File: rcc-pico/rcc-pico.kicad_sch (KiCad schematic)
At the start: 24 parts, among them J1 PJ-006A, J2 Conn_01x03_Female, SW1 SW_Push, U1 AP63300WU-7, U2 PicoW, U3 Conn_03x20, U4 Conn_03x20

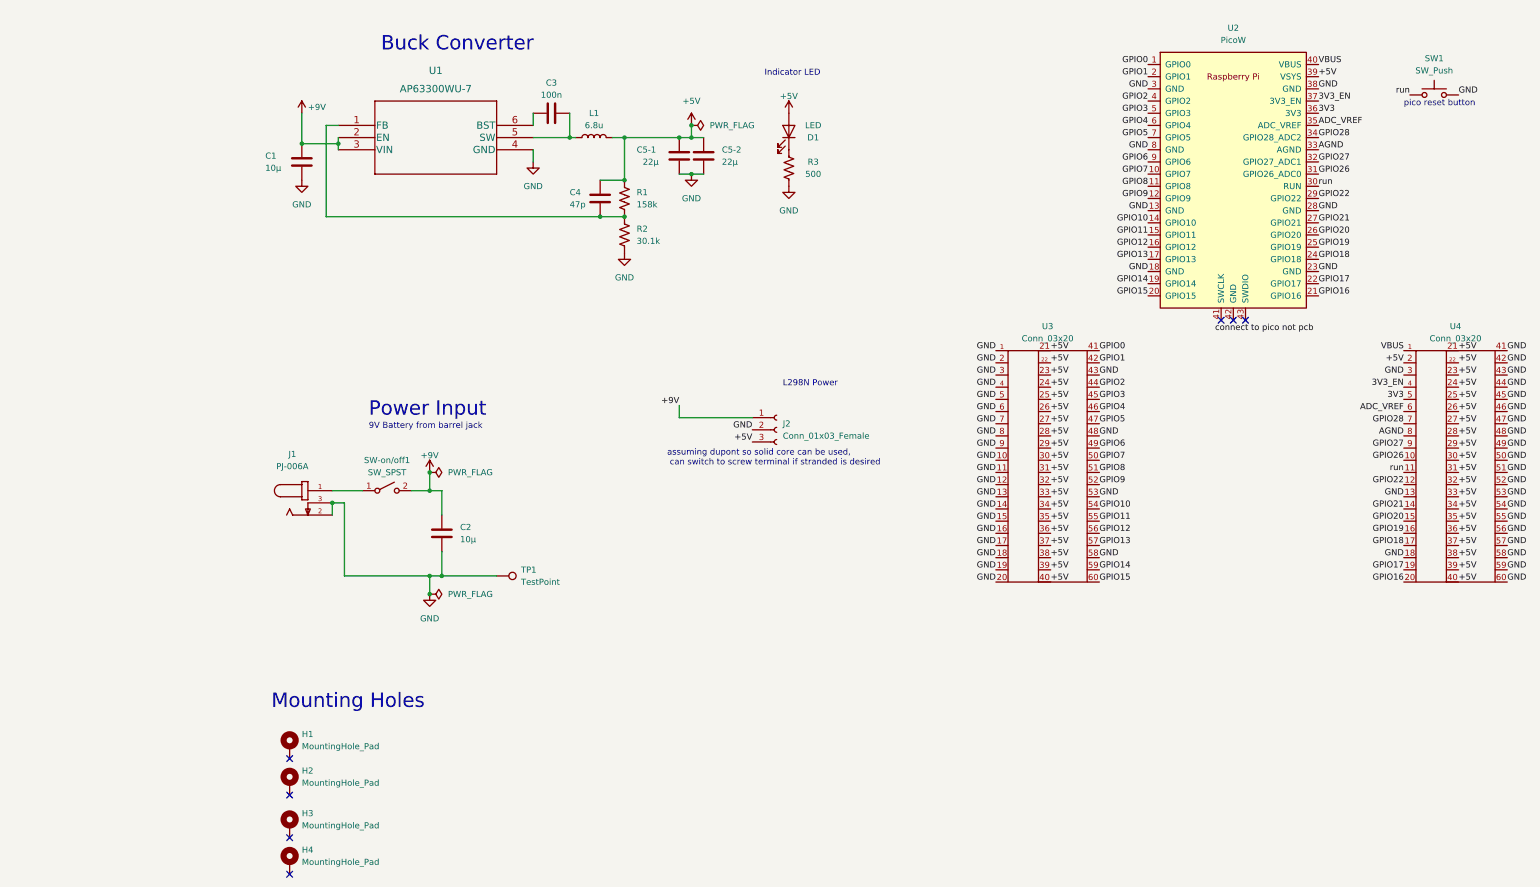
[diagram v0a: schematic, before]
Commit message: new schematic with LDO
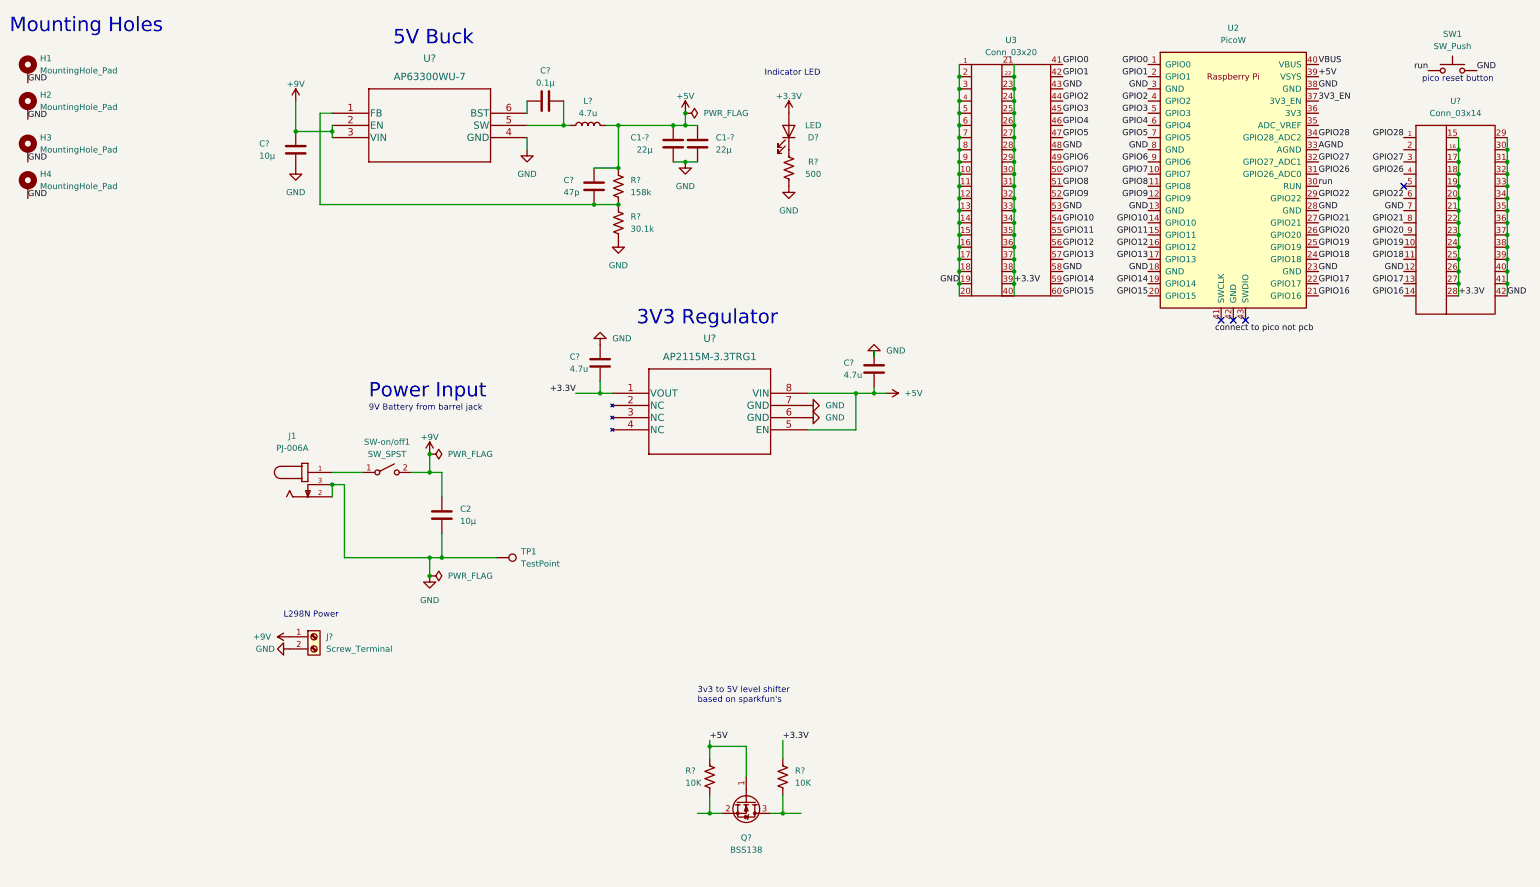
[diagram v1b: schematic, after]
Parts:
- removed C1: 10μ, Capacitor_SMD:C_1210_3225Metric_Pad1.33x2.70mm_HandSolder, symbol Device:C
- removed C3: 100n, Capacitor_SMD:C_1206_3216Metric_Pad1.33x1.80mm_HandSolder, symbol Device:C
- removed C4: 47p, Capacitor_SMD:C_0603_1608Metric_Pad1.08x0.95mm_HandSolder, symbol Device:C
- removed C5-1, C5-2: 22μ, Capacitor_SMD:C_1210_3225Metric_Pad1.33x2.70mm_HandSolder, symbol Device:C
- removed D1: LED, LED_SMD:LED_0603_1608Metric, symbol Device:LED
- removed J2: Conn_01x03_Female, Connector_PinHeader_2.54mm:PinHeader_1x03_P2.54mm_Vertical, symbol Connector:Conn_01x03_Female
- removed L1: 6.8u, Inductor_SMD:L_Wuerth_HCI-1365, symbol Device:L
- removed R1: 158k, Resistor_SMD:R_0805_2012Metric_Pad1.20x1.40mm_HandSolder, symbol Device:R_US
- removed R2: 30.1k, Resistor_SMD:R_1206_3216Metric, symbol Device:R_US
- removed R3: 500, Resistor_SMD:R_0603_1608Metric, symbol Device:R_US
- removed U1: AP63300WU-7, Package_TO_SOT_SMD:TSOT-23-6_HandSoldering, symbol ultralibrarian:AP63300WU-7
- removed U4: Conn_03x20, 3rdparty:PinHeader_3x20_P2.54mm_Vertical, symbol Connector:Conn_03x20
- added C1-? (x2): 22μ, Capacitor_SMD:C_1210_3225Metric_Pad1.33x2.70mm_HandSolder, symbol Device:C
- added C?: 10μ, Capacitor_SMD:C_1210_3225Metric_Pad1.33x2.70mm_HandSolder, symbol Device:C
- added C?: 0.1μ, Capacitor_SMD:C_1206_3216Metric_Pad1.33x1.80mm_HandSolder, symbol Device:C
- added C? (x2): 4.7u, Capacitor_SMD:C_0603_1608Metric_Pad1.08x0.95mm_HandSolder, symbol Device:C
- added C?: 47p, Capacitor_SMD:C_0603_1608Metric_Pad1.08x0.95mm_HandSolder, symbol Device:C
- added D?: LED, LED_SMD:LED_0603_1608Metric, symbol Device:LED
- added J?: Screw_Terminal, TerminalBlock_4Ucon:TerminalBlock_4Ucon_1x02_P3.50mm_Horizontal, symbol Connector:Screw_Terminal_01x02
- added L?: 4.7u, Inductor_SMD:SIDMP-SP0530, symbol Device:L
- added Q?: BSS138, Package_TO_SOT_SMD:SOT-23, symbol Transistor_FET:BSS138
- added R?: 500, Resistor_SMD:R_0603_1608Metric, symbol Device:R_US
- added R?: 158k, Resistor_SMD:R_0805_2012Metric_Pad1.20x1.40mm_HandSolder, symbol Device:R_US
- added R?: 30.1k, Resistor_SMD:R_1206_3216Metric, symbol Device:R_US
- added R? (x2): 10K, Resistor_SMD:R_1206_3216Metric, symbol Device:R_US
- added U?: AP2115M-3.3TRG1, Package_SO:AP2115M-3.3TRG1, symbol Regulator_Linear:AP2115M-3.3TRG1
- added U?: Conn_03x14, symbol Connector:Conn_03x14
- added U?: AP63300WU-7, Package_TO_SOT_SMD:TSOT-23-6_HandSoldering, symbol ultralibrarian:AP63300WU-7
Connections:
- net +5V: now also C1-?.1, C1-?.1, C?.1, C?.2, L?.2, Q?.1 (G), R?.1, R?.2, U?.5 (EN), U?.8 (VIN); no longer U3.21, U3.22, U3.23, U3.24, U3.25, U3.26, U3.27, U3.28, U3.29, U3.30, U3.31, U3.32, U3.33, U3.34, U3.35, U3.36, U3.37, U3.38, U3.39, U3.40
- net +9V: now also C?.1, J?.1 (Pin_1), U?.2 (EN), U?.3 (VIN)
- net GND: now also H1.1, H2.1, H3.1, H4.1, C1-?.2, C1-?.2, C?.2, C?.2, C?.2, J?.2 (Pin_2), R?.2, R?.2, U?.12, U?.29, U?.30, U?.31, U?.32, U?.33, U?.34, U?.35, U?.36, U?.37, U?.38, U?.39, U?.4 (GND), U?.40, U?.41, U?.42, U?.6 (GND), U?.7, U?.7 (GND)
- net GPIO16: now also U?.14
- net GPIO17: now also U?.13
- net GPIO18: now also U?.11
- net GPIO19: now also U?.10
- net GPIO20: now also U?.9
- net GPIO21: now also U?.8
- net GPIO22: now also U?.6
- net GPIO26: now also U?.4
- net GPIO27: now also U?.3
- net GPIO28: now also U?.1
- net 3V3: no longer names the net of U2.36 (3V3)
- net ADC_VREF: no longer names the net of U2.35 (ADC_VREF)
- new net: Q?.2 (S), R?.2
- new net: Q?.3 (D), R?.2
- new net: C?.2, L?.1, U?.5 (SW)
- new net: D?.1 (K), R?.1
- new net: C?.1, R?.1, R?.1, U?.1 (FB)
- new net: C?.1, U?.6 (BST)
- new net +3.3V: C?.1, D?.2 (A), R?.1, U3.21, U3.22, U3.23, U3.24, U3.25, U3.26, U3.27, U3.28, U3.29, U3.30, U3.31, U3.32, U3.33, U3.34, U3.35, U3.36, U3.37, U3.38, U3.39, U3.40, U?.1 (VOUT), U?.15, U?.16, U?.17, U?.18, U?.19, U?.20, U?.21, U?.22, U?.23, U?.24, U?.25, U?.26, U?.27, U?.28
- no-connect marks 7 -> 4
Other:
- note added: "3V3 Regulator"
- note added: "3v3 to 5V level shifter based on sparkfun's"
- note added: "5V Buck"
- note removed: "Buck Converter"
- note removed: "assuming dupont so solid core can be used, can switch to screw terminal if stranded is desired"
- moved on the sheet: C2, H1, H2, H3, H4, J1, SW-on/off1, SW1, TP1, U3

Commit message: finished schematic
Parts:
- added J10: Conn_3x3_female, Connector_PinHeader_2.54mm:PinHeader3x3_P2.54mm_Vertical, symbol Connector:Conn_3x3_female
- added J3, J7: Conn_02x03_Top_Bottom, Connector_PinHeader_2.54mm:PinHeader_2x03_P2.54mm_Vertical, symbol Connector_Generic:Conn_02x03_Odd_Even
- added J4, J6: Conn_03x3_female, Connector_PinHeader_2.54mm:PinHeader3x3_P2.54mm_Vertical, symbol Connector:Conn_03x3_female
- added J8: Conn_04x4, Connector_PinHeader_2.54mm:PinHeader4x4_P_2.54mm_Vertical, symbol Connector:Conn_04x4
- added J9: Conn_02x02_Top_Bottom, Connector_PinHeader_2.54mm:PinHeader_2x02_P2.54mm_Vertical, symbol Connector_Generic:Conn_02x02_Odd_Even
- added Q2, Q3: BSS138, Package_TO_SOT_SMD:SOT-23, symbol Transistor_FET:BSS138
- added R6, R7, R8, R9: 10K, Resistor_SMD:R_0402_1005Metric, symbol Device:R_US
- added SW-on/off2: SW_SPST, 3rdparty:SW-T2-4E-B-A2-MA2, symbol Switch:SW_SPST
- J1: footprint CUI_PJ-006A -> 3rdparty:CUI_PJ-006A
- J2: renamed from J?; footprint TerminalBlock_4Ucon:TerminalBlock_4Ucon_1x02_P3.50mm_Horizontal -> TerminalBlock_Phoenix:TerminalBlock_Phoenix_MPT-0,5-2-2.54_1x02_P2.54mm_Horizontal
- J5: renamed from U?; value Conn_03x14 -> Conn_03x9; footprint (none) -> 3rdparty:PinHeader_3x9_P2.54mm_Vertical; symbol Connector:Conn_03x14 -> Connector:Conn_03x9
- R3, R4: renamed from R?; footprint Resistor_SMD:R_1206_3216Metric -> Resistor_SMD:R_0402_1005Metric
- gave numbers to parts that had none: 15
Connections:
- net AGND is gone; now on net GND: U2.33 (AGND)
- net +3.3V: now also J5.10, J5.11, J5.12, J5.13, J5.14, J10.4, J10.5, J10.6, J6.1, J6.2, J6.3, J8.1, J8.2, J8.3, J8.4, R7.1, R9.1; no longer J5.19, J5.20, J5.21, J5.22, J5.23, J5.24, J5.25, J5.26, J5.27, J5.28
- net +5V: now also J4.4, J4.5, J4.6, Q2.1 (G), Q3.1 (G), R6.1, R8.1
- net +9V: now also SW-on/off2.2 (B); no longer J2.1 (Pin_1)
- net GND: now also J5.1, J5.2, J5.20, J5.25, J5.3, J5.4, J5.5, J5.6, J5.8, J5.9, U3.41, U3.42, U3.44, U3.45, U3.46, U3.47, U3.49, U3.50, U3.51, U3.52, U3.54, U3.55, U3.56, U3.57, U3.59, U3.60, J10.1, J10.2, J10.3, J4.1, J4.2, J4.3, J6.7, J6.8, J6.9, J8.5, J8.6, J8.7, J8.8; no longer J5.12, J5.29, J5.30, J5.31, J5.32, J5.33, J5.34, J5.35, J5.36, J5.37, J5.38, J5.39, J5.40, J5.41, J5.42, U3.1, U3.10, U3.11, U3.12, U3.14, U3.15, U3.16, U3.17, U3.19, U3.2, U3.20, U3.4, U3.5, U3.6, U3.7, U3.9
- net GPIO0: now also U3.1; no longer U3.41
- net GPIO1: now also U3.2; no longer U3.42
- net GPIO10: now also U3.14; no longer U3.54
- net GPIO11: now also U3.15, J3.1 (Pin_1); no longer U3.55
- net GPIO12: now also U3.16, J3.3 (Pin_3); no longer U3.56
- net GPIO13: now also U3.17, J3.5 (Pin_5); no longer U3.57
- net GPIO14: now also U3.19, J9.1 (Pin_1); no longer U3.59
- net GPIO15: now also U3.20, J9.3 (Pin_3); no longer U3.60
- net GPIO16: now also J5.27; no longer J5.14
- net GPIO17: now also J5.26; no longer J5.13
- net GPIO18: now also J5.24; no longer J5.11
- net GPIO19: now also J5.23; no longer J5.10
- net GPIO2: now also U3.4; no longer U3.44
- net GPIO20: now also J5.22; no longer J5.9
- net GPIO21: now also J5.21; no longer J5.8
- net GPIO22: now also J5.19; no longer J5.6
- net GPIO26: now also J10.9, J7.5 (Pin_5); no longer J5.4
- net GPIO27: now also J10.8, J7.3 (Pin_3); no longer J5.3
- net GPIO28: now also J10.7, J7.1 (Pin_1); no longer J5.1
- net GPIO3: now also U3.5; no longer U3.45
- net GPIO4: now also U3.6; no longer U3.46
- net GPIO5: now also U3.7; no longer U3.47
- net GPIO6: now also U3.9; no longer U3.49
- net GPIO7: now also U3.10; no longer U3.50
- net GPIO8: now also U3.11; no longer U3.51
- net GPIO9: now also U3.12; no longer U3.52
- net 5V_PWM_1: now reaches Q1.2 (S), R3.2
- net 5V_PWM_1: now also J4.7
- net 3V3_PWM_1: now reaches Q1.3 (D), R4.2
- net 3V3_PWM_1: now also J3.2 (Pin_2)
- net 3V3_EN: no longer names the net of U2.37 (3V3_EN)
- net VBUS: no longer names the net of U2.40 (VBUS)
- new net 3V3_PWM_2: J3.4 (Pin_4), Q2.3 (D), R7.2
- new net 3V3_PWM_3: J3.6 (Pin_6), Q3.3 (D), R9.2
- new net 5V_PWM_2: J4.8, Q2.2 (S), R6.2
- new net 5V_PWM_3: J4.9, Q3.2 (S), R8.2
- new net ADC0: J6.4, J7.2 (Pin_2)
- new net ADC1: J6.5, J7.4 (Pin_4)
- new net ADC2: J6.6, J7.6 (Pin_6)
- new net MTRPWR: J2.1 (Pin_1), SW-on/off2.1 (A)
- new net SCL: J8.10, J8.11, J8.12, J8.9, J9.4 (Pin_4)
- new net SDA: J8.13, J8.14, J8.15, J8.16, J9.2 (Pin_2)
- no-connect marks 4 -> 7
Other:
- note added: "3v3 to 5V level shifter"
- note added: "ADC Activate"
- note added: "ADC expansion"
- note added: "I2C1 Activate"
- note added: "I2C1 expansion"
- note added: "L298N POWER"
- note added: "Servo Activate"
- note added: "Servo Connection *note 5V PWM"
- note added: "based on sparkfun's"
- note added: "gpio options for I2C1 bus SCL: 3 7 11 15 19 SDA: 2 6 10 14 18"
- note added: "leaving unconnected so switch must be on to power the devices, not all from pico"
- note added: "notes: SPI1, I2C0, UART0 used for wifi going to breakout I2C1"
- note added: "options for PWM 0 1 4 5 8 9 12 13 16 17 20 21 22"
- note added: "this allows for gpio to be used and expansion pins to be used *must activate breakouts to only use one at a time"
- note removed: "3v3 to 5V level shifter based on sparkfun's"
- moved on the sheet: C2, H1, H2, H3, H4, J1, J2, Q1, R3, R4, SW-on/off1, SW1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

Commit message: finished schematic and layout
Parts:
- removed J3, J7: Conn_02x03_Top_Bottom, Connector_PinHeader_2.54mm:PinHeader_2x03_P2.54mm_Vertical, symbol Connector_Generic:Conn_02x03_Odd_Even
- removed J6: Conn_03x3_female, Connector_PinHeader_2.54mm:PinHeader3x3_P2.54mm_Vertical, symbol Connector:Conn_03x3_female
- removed J9: Conn_02x02_Top_Bottom, Connector_PinHeader_2.54mm:PinHeader_2x02_P2.54mm_Vertical, symbol Connector_Generic:Conn_02x02_Odd_Even
- added J4: Conn_3x4_female, 3rdparty:PinHeader_3x4_P2.54mm_vertical, symbol Connector:Conn_3x4_female
- added J6: Conn_02x04_Top_Bottom, Connector_PinHeader_2.54mm:PinHeader_2x04_P2.54mm_Vertical, symbol Connector_Generic:Conn_02x04_Top_Bottom
- C1: renamed from C2; footprint Capacitor_SMD:C_1210_3225Metric_Pad1.33x2.70mm_HandSolder -> Capacitor_SMD:C_0805_2012Metric
- C2: renamed from C1; footprint Capacitor_SMD:C_1210_3225Metric_Pad1.33x2.70mm_HandSolder -> Capacitor_SMD:C_0805_2012Metric
- C3: footprint Capacitor_SMD:C_1206_3216Metric_Pad1.33x1.80mm_HandSolder -> Capacitor_SMD:C_0402_1005Metric
- C4: footprint Capacitor_SMD:C_0603_1608Metric_Pad1.08x0.95mm_HandSolder -> Capacitor_SMD:C_0603_1608Metric
- C5: renamed from C1-1; footprint Capacitor_SMD:C_1210_3225Metric_Pad1.33x2.70mm_HandSolder -> Capacitor_SMD:C_0805_2012Metric
- C6: renamed from C1-2; footprint Capacitor_SMD:C_1210_3225Metric_Pad1.33x2.70mm_HandSolder -> Capacitor_SMD:C_0805_2012Metric
- C7: renamed from C5; footprint Capacitor_SMD:C_0603_1608Metric_Pad1.08x0.95mm_HandSolder -> Capacitor_SMD:C_0402_1005Metric
- C8: renamed from C6; footprint Capacitor_SMD:C_0603_1608Metric_Pad1.08x0.95mm_HandSolder -> Capacitor_SMD:C_0402_1005Metric
- J2: footprint TerminalBlock_Phoenix:TerminalBlock_Phoenix_MPT-0,5-2-2.54_1x02_P2.54mm_Horizontal -> TerminalBlock:TCxx03_5mm_2x1
- J5: renamed from U3; value Conn_03x20 -> Conn_03x10; footprint 3rdparty:PinHeader_3x20_P2.54mm_Vertical -> 3rdparty:PinHeader_3x11_P2.54mm_Vertical; symbol Connector:Conn_03x20 -> Connector:Conn_03x10
- J9: renamed from J5; footprint 3rdparty:PinHeader_3x9_P2.54mm_Vertical -> 3rdparty:PinHeader3x7+3
- L1: footprint Inductor_SMD:SIDMP-SP0530 -> Inductor_SMD:BWVS00606045
- R1: footprint Resistor_SMD:R_0805_2012Metric_Pad1.20x1.40mm_HandSolder -> Resistor_SMD:R_0402_1005Metric
- R2: footprint Resistor_SMD:R_1206_3216Metric -> Resistor_SMD:R_0402_1005Metric
- R3: renamed from R5; value 500 -> 470; footprint Resistor_SMD:R_0603_1608Metric -> Resistor_SMD:R_0402_1005Metric
- SW-on/off1, SW-on/off2: footprint 3rdparty:SW-T2-4E-B-A2-MA2 -> 3rdparty:SW-T3-2B-A-A3-S1
- U1: footprint Package_TO_SOT_SMD:TSOT-23-6_HandSoldering -> Package_TO_SOT_SMD:TSOT-23-6
- renumbered J4 to J3, J8 to J7, J10 to J8, R3 to R4, R4 to R5, U4 to U2, U2 to U3
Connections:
- net +3.3V: now also J5.11, J5.12, J5.13, J5.14, J5.15, J5.16, J5.17, J5.18, J5.19, J5.20, J9.8, J9.9, J4.5, J4.6, J4.7, J4.8, J6.5, J6.6; no longer J5.21, J5.22, J5.23, J5.24, J5.25, J5.26, J5.27, J5.28, J5.29, J5.30, J5.31, J5.32, J5.33, J5.34, J5.35, J5.36, J5.37, J5.38, J5.39, J5.40, J9.15, J9.16, J9.17, J9.18
- net 3V3_PWM_1: now also J9.22
- net 3V3_PWM_2: now also J9.23
- net 3V3_PWM_3: now also J9.24
- net GND: now also J5.21, J5.22, J5.23, J5.24, J5.25, J5.26, J5.27, J5.28, J5.29, J5.30, J4.10, J4.11, J4.12, J4.9, J6.7, J6.8 (Pin_8); no longer J5.13, J5.18, J5.3, J5.41, J5.42, J5.43, J5.44, J5.45, J5.46, J5.47, J5.48, J5.49, J5.50, J5.51, J5.52, J5.53, J5.54, J5.55, J5.56, J5.57, J5.58, J5.59, J5.60, J5.8, J9.20, J9.25, J9.8, J9.9
- net GPIO0: now also J4.1; no longer J5.1
- net GPIO1: now also J4.2; no longer J5.2
- net GPIO10: now also J5.7; no longer J5.14
- net GPIO11: now also J5.8; no longer J5.15
- net GPIO12: now also J5.9; no longer J5.16
- net GPIO13: now also J5.10; no longer J5.17
- net GPIO14: now also J6.4; no longer J5.19
- net GPIO15: now also J6.3 (Pin_3); no longer J5.20
- net GPIO16: now also J9.21; no longer J9.27
- net GPIO17: now also J9.20; no longer J9.26
- net GPIO18: now also J9.19; no longer J9.24
- net GPIO19: now also J9.18; no longer J9.23
- net GPIO2: now also J4.3; no longer J5.4
- net GPIO20: now also J9.17; no longer J9.22
- net GPIO21: now also J9.16; no longer J9.21
- net GPIO22: now also J9.15; no longer J9.19
- net GPIO3: now also J4.4; no longer J5.5
- net GPIO4: now also J5.1; no longer J5.6
- net GPIO5: now also J5.2; no longer J5.7
- net GPIO6: now also J5.3; no longer J5.9
- net GPIO7: now also J5.4; no longer J5.10
- net GPIO8: now also J5.5; no longer J5.11
- net GPIO9: now also J5.6; no longer J5.12
- net SCL: now also J6.1
- net SDA: now also J6.2
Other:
- note added: "Servo Activate 5V PWM activate"
- note removed: "ADC Activate"
- note removed: "ADC expansion"
- note removed: "Servo Activate"
- moved on the sheet: C1, C7, C8, D1, H2, H3, H4, J1, Q1, Q2, Q3, R3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

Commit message: ordered JLC
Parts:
- removed J7: Conn_04x4, Connector_PinHeader_2.54mm:PinHeader4x4_P_2.54mm_Vertical, symbol Connector:Conn_04x4
- added C9: 0.1μ, Capacitor_SMD:C_0402_1005Metric, symbol Device:C
- added J10, J7: Conn_02x04_Top_Bottom, Connector_PinHeader_2.54mm:PinHeader_2x04_P2.54mm_Vertical-down, symbol Connector_Generic:Conn_02x04_Top_Bottom
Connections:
- net +3.3V: now also J10.4 (Pin_4), J10.8 (Pin_8), J7.4 (Pin_4), J7.8 (Pin_8)
- net +5V: now also C9.2
- net GND: now also C9.1, J10.3 (Pin_3), J10.7 (Pin_7), J7.3 (Pin_3), J7.7 (Pin_7)
- net SCL: now also J10.2 (Pin_2), J10.6 (Pin_6), J7.2 (Pin_2), J7.6 (Pin_6)
- net SDA: now also J10.1 (Pin_1), J10.5 (Pin_5), J7.1 (Pin_1), J7.5 (Pin_5)
